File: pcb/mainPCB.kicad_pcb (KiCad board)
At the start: 4 copper layers, 160 x 73.2 mm, 164 parts, among them IC1 FXL6408UMX, IC2 ATA6561-GAQW-N, IC3 ICL3221EIVZ, J1 PTSM-Header-Horizontal-6, J10 Conn_01x08_Female, J11 Conn_01x08_Female, J12 Conn_02x02_Odd_Even, J13 SM04B-SRSS-TB(LF)(SN), J14 USB_B_Micro, J15 RJ45_Amphenol_RJMG1BD3B8K1ANR, J16 DB9_Male_MountingHoles, J17 SM04B-SRSS-TB(LF)(SN), J18 PTSM-Header-Horizontal-2, J3 PTSM-Header-Horizontal-7, J4 CCA-Header-Horizontal-4, J5 PTSM-Header-Horizontal-5, J7 Conn_01x04_Male, J8 Conn_01x04_Male, J9 Conn_01x08_Female, K1 CP1SA-12V-Z, K2 CP1SA-12V-Z, Q1 BC817-40,215, Q2 BC817-40,215, SW1 SW_Push, U1 ESP32-WROOM-32, U10 NUD3124LT1G, U11 LAN8720A, U12 LSM9DS1, U2 AZ1117-3.3, U3 VNH7070AS, U4 ADS1115IDGS, U5 VNH7070AS, U6 PCA9306DCTR, U7 TPD3E001DRLR, U8 CP2102N-A01-GQFN24, U9 VNH7070AS

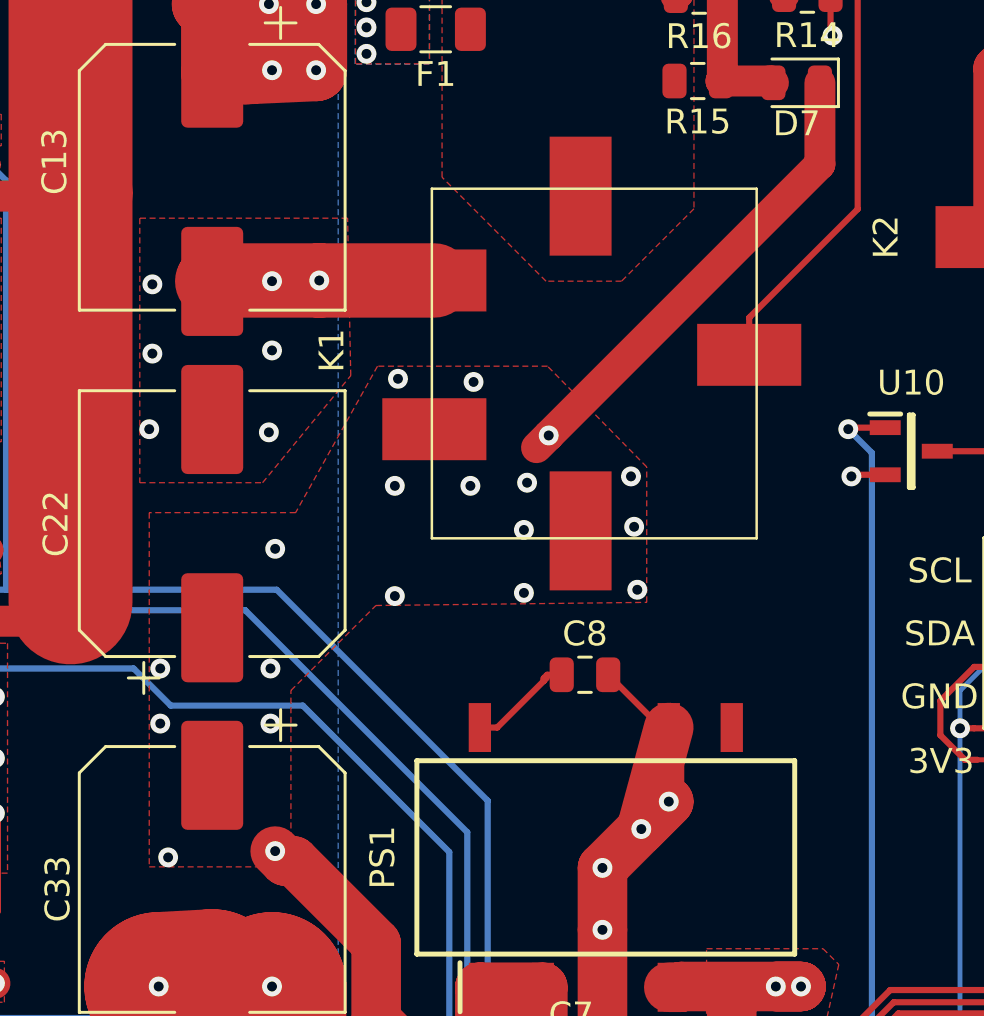
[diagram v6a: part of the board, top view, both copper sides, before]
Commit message: A few more vias for the main 12V input (top layer -> third layer)
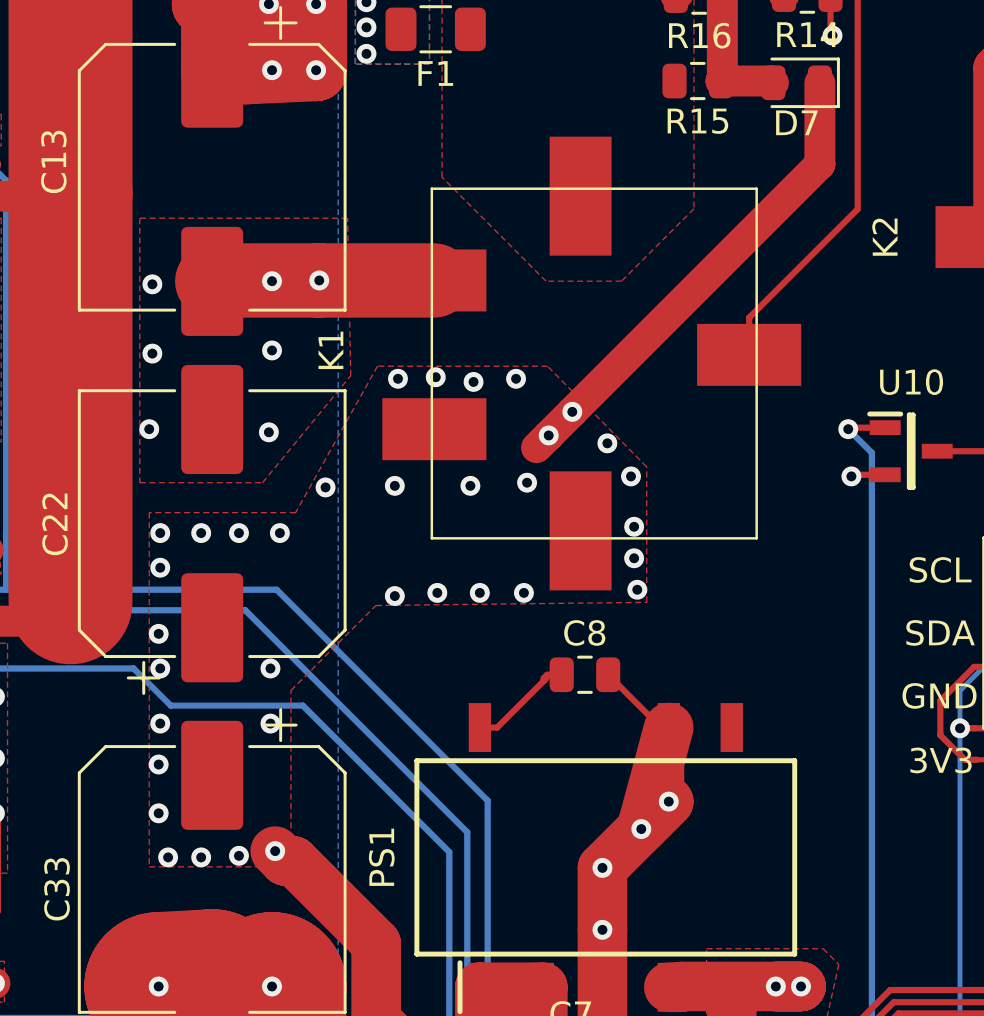
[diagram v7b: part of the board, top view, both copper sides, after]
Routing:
- net +12V: vias 44 -> 60
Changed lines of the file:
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@@
     (thickness 1.6)
     (drawings 57)
-    (tracks 1778)
+    (tracks 1795)
     (zones 0)
     (modules 164)
@@
   (segment (start 73.438001 81.686503) (end 73.438001 80.295499) (width 0.25) (layer F.Cu) (net 5))
   (segment (start 77.1145 78.9305) (end 74.803 78.9305) (width 0.25) (layer F.Cu) (net 5))
-  (segment (start 68.58 58.656998) (end 57.640998 69.596) (width 1.25) (layer F.Cu) (net 6))
+  (segment (start 68.58 58.656998) (end 58.593498 68.6435) (width 1.25) (layer F.Cu) (net 6))
   (segment (start 68.58 55.372) (end 68.58 58.656998) (width 1.25) (layer F.Cu) (net 6))
   (via (at 89.281 67.437) (size 0.8) (drill 0.4) (layers F.Cu B.Cu) (net 6))
@@
   (via (at 54.483 71.628) (size 0.8) (drill 0.4) (layers F.Cu B.Cu) (net 6))
   (via (at 56.769 71.501) (size 0.8) (drill 0.4) (layers F.Cu B.Cu) (net 6))
-  (via (at 56.642 73.406) (size 0.8) (drill 0.4) (layers F.Cu B.Cu) (net 6))
   (via (at 56.642 75.946) (size 0.8) (drill 0.4) (layers F.Cu B.Cu) (net 6))
   (via (at 51.435 76.073) (size 0.8) (drill 0.4) (layers F.Cu B.Cu) (net 6))
@@
   (via (at 42.291 86.614) (size 0.8) (drill 0.4) (layers F.Cu B.Cu) (net 6))
   (via (at 46.609 86.36) (size 0.8) (drill 0.4) (layers F.Cu B.Cu) (net 6))
-  (via (at 46.609 74.168) (size 0.8) (drill 0.4) (layers F.Cu B.Cu) (net 6))
+  (via (at 46.7995 73.533) (size 0.8) (drill 0.4) (layers F.Cu B.Cu) (net 6))
   (segment (start 45.419 54.982) (end 46.482 54.864) (width 2.5) (layer F.Cu) (net 6))
   (segment (start 44.069 54.982) (end 45.419 54.982) (width 2.5) (layer F.Cu) (net 6))
@@
   (via (at 46.4185 81.2165) (size 0.8) (drill 0.4) (layers F.Cu B.Cu) (net 6))
   (via (at 41.9735 81.2165) (size 0.8) (drill 0.4) (layers F.Cu B.Cu) (net 6))
+  (via (at 41.9735 73.533) (size 0.8) (drill 0.4) (layers F.Cu B.Cu) (net 6))
+  (via (at 43.6245 73.533) (size 0.8) (drill 0.4) (layers F.Cu B.Cu) (net 6))
+  (via (at 45.1485 73.533) (size 0.8) (drill 0.4) (layers F.Cu B.Cu) (net 6))
+  (via (at 48.641 71.6915) (size 0.8) (drill 0.4) (layers F.Cu B.Cu) (net 6))
+  (via (at 53.086 67.2465) (size 0.8) (drill 0.4) (layers F.Cu B.Cu) (net 6))
+  (via (at 56.3245 67.31) (size 0.8) (drill 0.4) (layers F.Cu B.Cu) (net 6))
+  (segment (start 58.593498 68.6435) (end 57.640998 69.596) (width 1.25) (layer F.Cu) (net 6))
+  (via (at 58.593498 68.6435) (size 0.8) (drill 0.4) (layers F.Cu B.Cu) (net 6))
+  (via (at 60.0075 69.9135) (size 0.8) (drill 0.4) (layers F.Cu B.Cu) (net 6))
+  (via (at 54.864 75.946) (size 0.8) (drill 0.4) (layers F.Cu B.Cu) (net 6))
+  (via (at 53.1495 75.946) (size 0.8) (drill 0.4) (layers F.Cu B.Cu) (net 6))
+  (via (at 61.087 74.549) (size 0.8) (drill 0.4) (layers F.Cu B.Cu) (net 6))
+  (via (at 41.9735 74.93) (size 0.8) (drill 0.4) (layers F.Cu B.Cu) (net 6))
+  (via (at 41.91 77.597) (size 0.8) (drill 0.4) (layers F.Cu B.Cu) (net 6))
+  (via (at 41.91 82.8675) (size 0.8) (drill 0.4) (layers F.Cu B.Cu) (net 6))
+  (via (at 41.91 84.836) (size 0.8) (drill 0.4) (layers F.Cu B.Cu) (net 6))
+  (via (at 43.6245 86.614) (size 0.8) (drill 0.4) (layers F.Cu B.Cu) (net 6))
+  (via (at 45.1485 86.5505) (size 0.8) (drill 0.4) (layers F.Cu B.Cu) (net 6))
   (segment (start 66.04 103.983) (end 66.04 105.791) (width 0.25) (layer F.Cu) (net 7))
   (segment (start 69.342 103.983) (end 69.342 105.7425) (width 0.25) (layer F.Cu) (net 8))

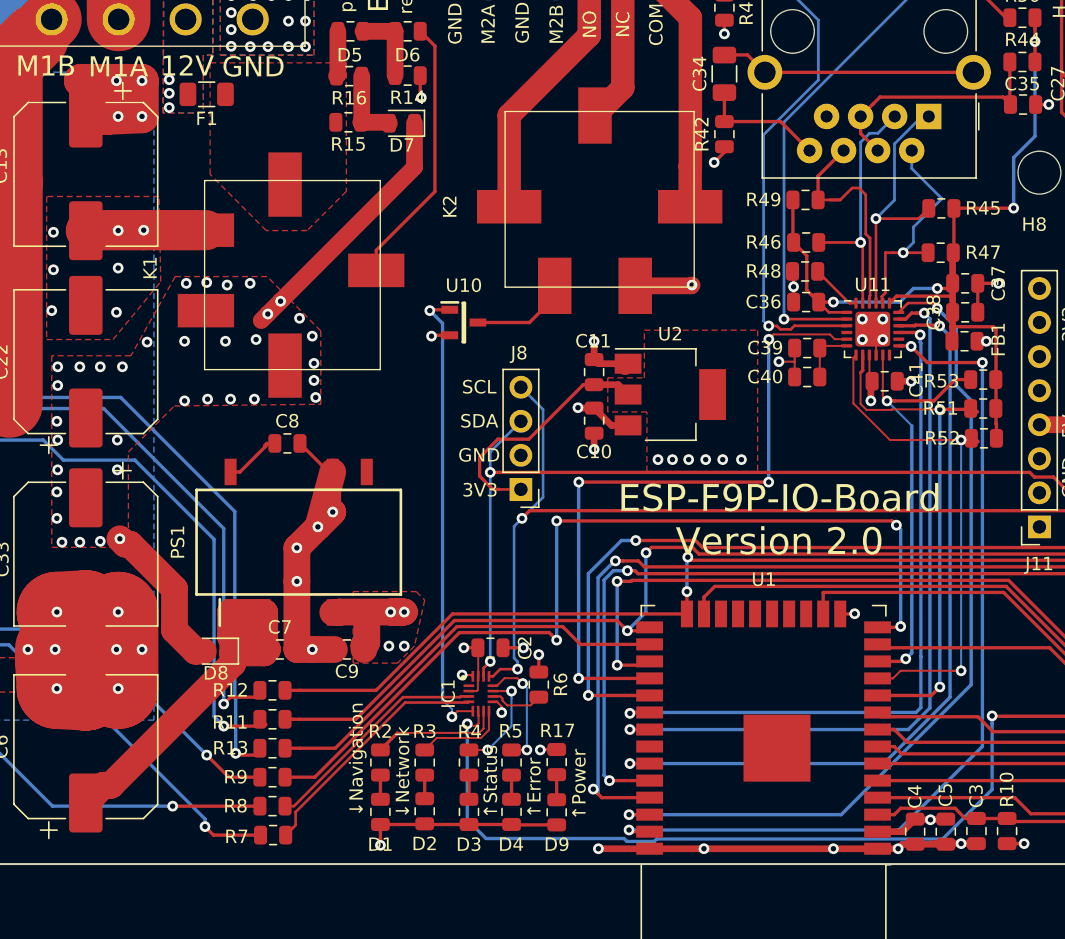
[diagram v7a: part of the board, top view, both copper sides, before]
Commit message: changed connection of the LAN8720A, RST to the FXL6408 and MDIO to the ESP32 (where RST was before). fixes #2
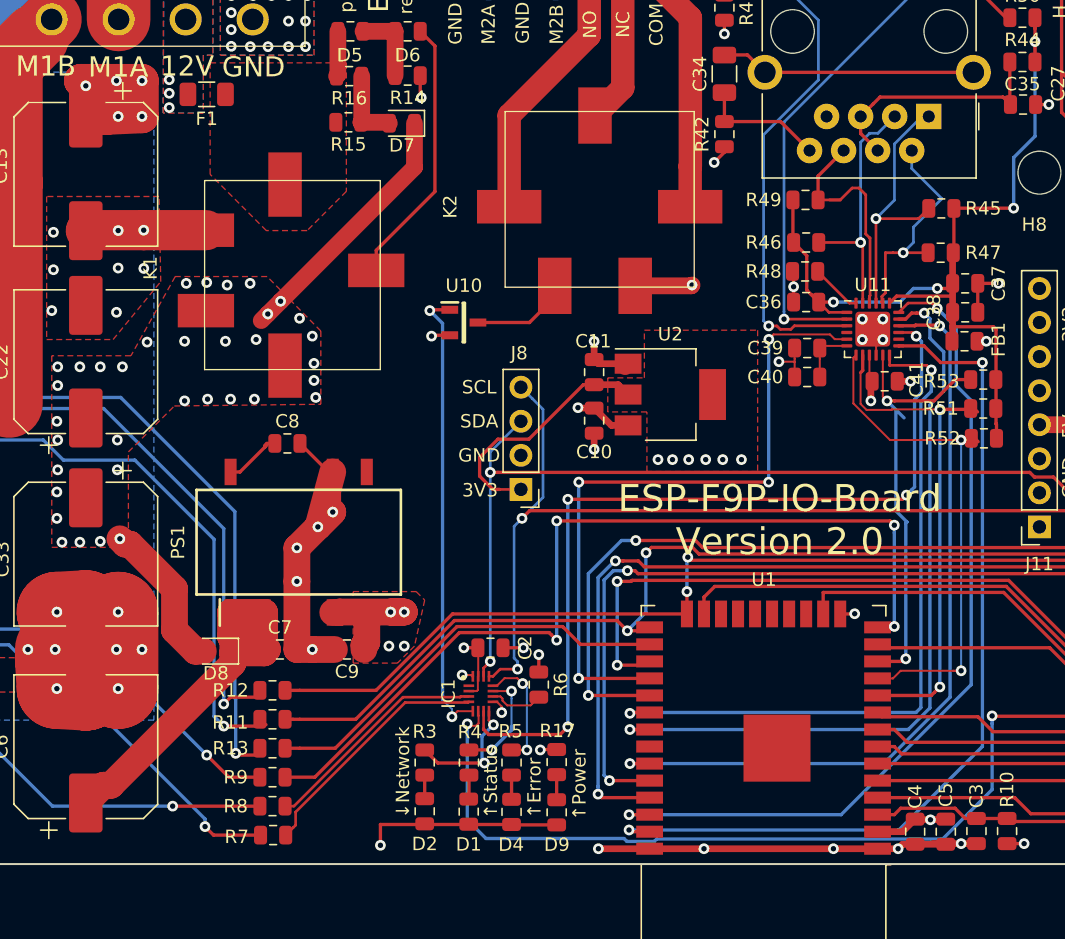
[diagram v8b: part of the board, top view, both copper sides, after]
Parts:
- removed D3: LED/green, Capacitor_SMD:C_0805_2012Metric
- removed R2: 620, Resistor_SMD:R_0805_2012Metric
- moved D1 6.58 mm to (72.6, 106.7)
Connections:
- IC1 pad 7: Net-(IC1-Pad7) -> /PHY_RST
- R4 pad 1: Net-(D3-Pad2) -> Net-(D1-Pad2)
- U1 pad 30: /LAN8720/PHY_RST: -> /LAN8720/MDIO
- U11 pad 12: Net-(U11-Pad12) -> /LAN8720/MDIO
- U11 pad 15: /LAN8720/PHY_RST: -> /PHY_RST
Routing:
- net /PHY_RST: track 0.00 -> 64.4 mm, vias 0 -> 4
- net /LAN8720/MDIO: track 0.00 -> 53.1 mm, vias 0 -> 2
- net /LAN8720/PHY_RST:: track 53.1 -> 0.00 mm, vias 2 -> 0
- net Net-(IC1-Pad7): track 9.67 -> 0.00 mm
- net Net-(IC1-Pad8): track 6.81 -> 9.29 mm, vias 0 -> 2
- net Net-(D3-Pad2): track 1.81 -> 0.00 mm
- net /usbUart/RX: track 117.2 -> 116.2 mm
- net /LAN8720/EMAC_TXD0:GPIO19: track 56.2 -> 57.1 mm
- net /M2_PWM: track 68.8 -> 68.0 mm
- net /LAN8720/EMAC_RX_CRS_DV:GPIO27: track 33.1 -> 33.6 mm
- net GND: track 283.0 -> 282.9 mm, vias 115 -> 116
- net /LAN8720/MDC:GPIO23: vias 3 -> 2
- net +12V: vias 60 -> 61
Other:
- board text removed: "↓Navigation"
